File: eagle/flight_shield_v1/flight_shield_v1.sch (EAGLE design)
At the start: 16 parts

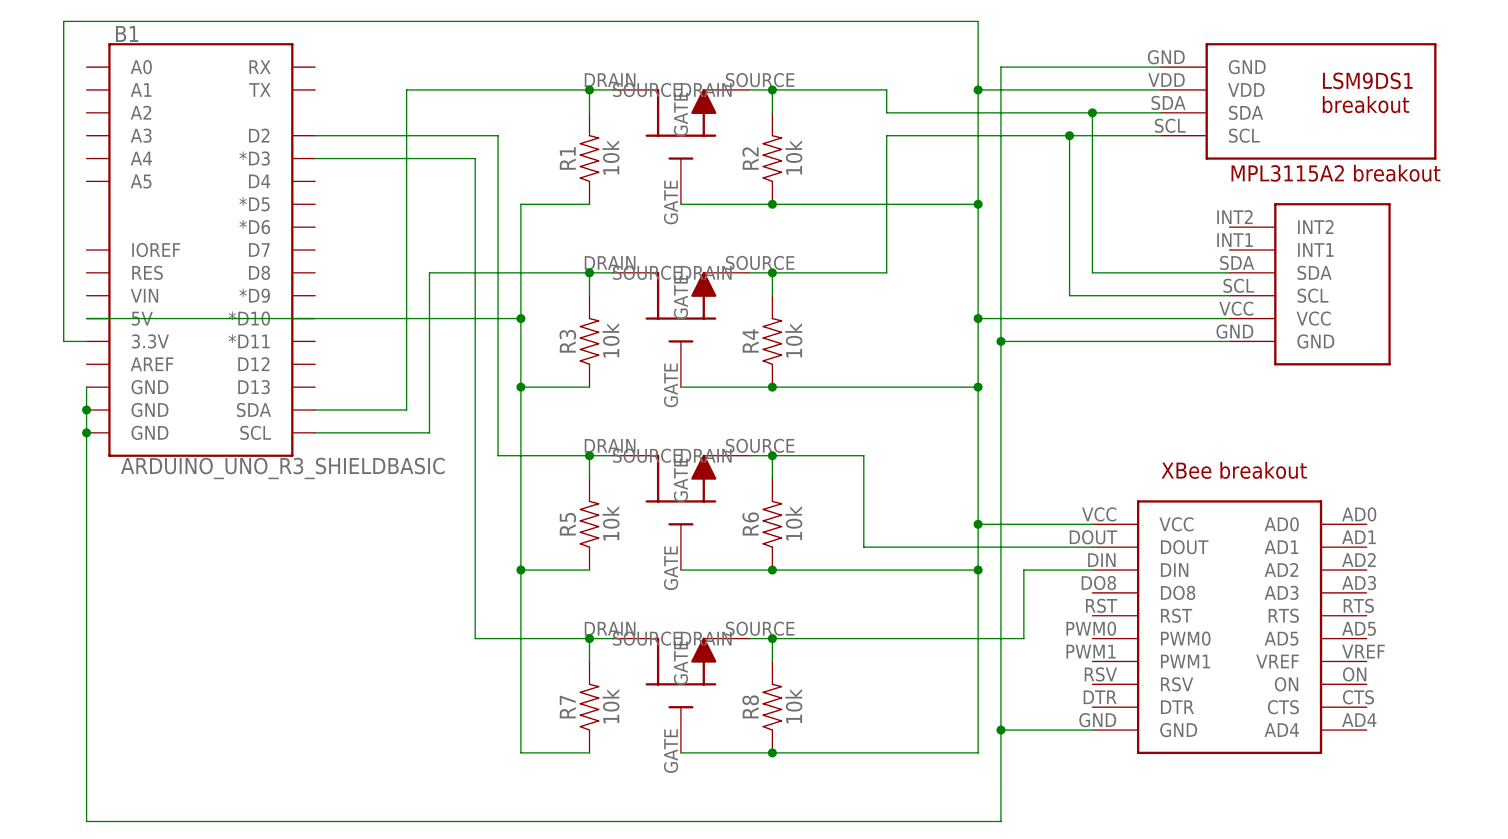
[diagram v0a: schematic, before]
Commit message: IMU / AHRS prosessering begynner å bli bedre. Flyttet arduino filer til git.
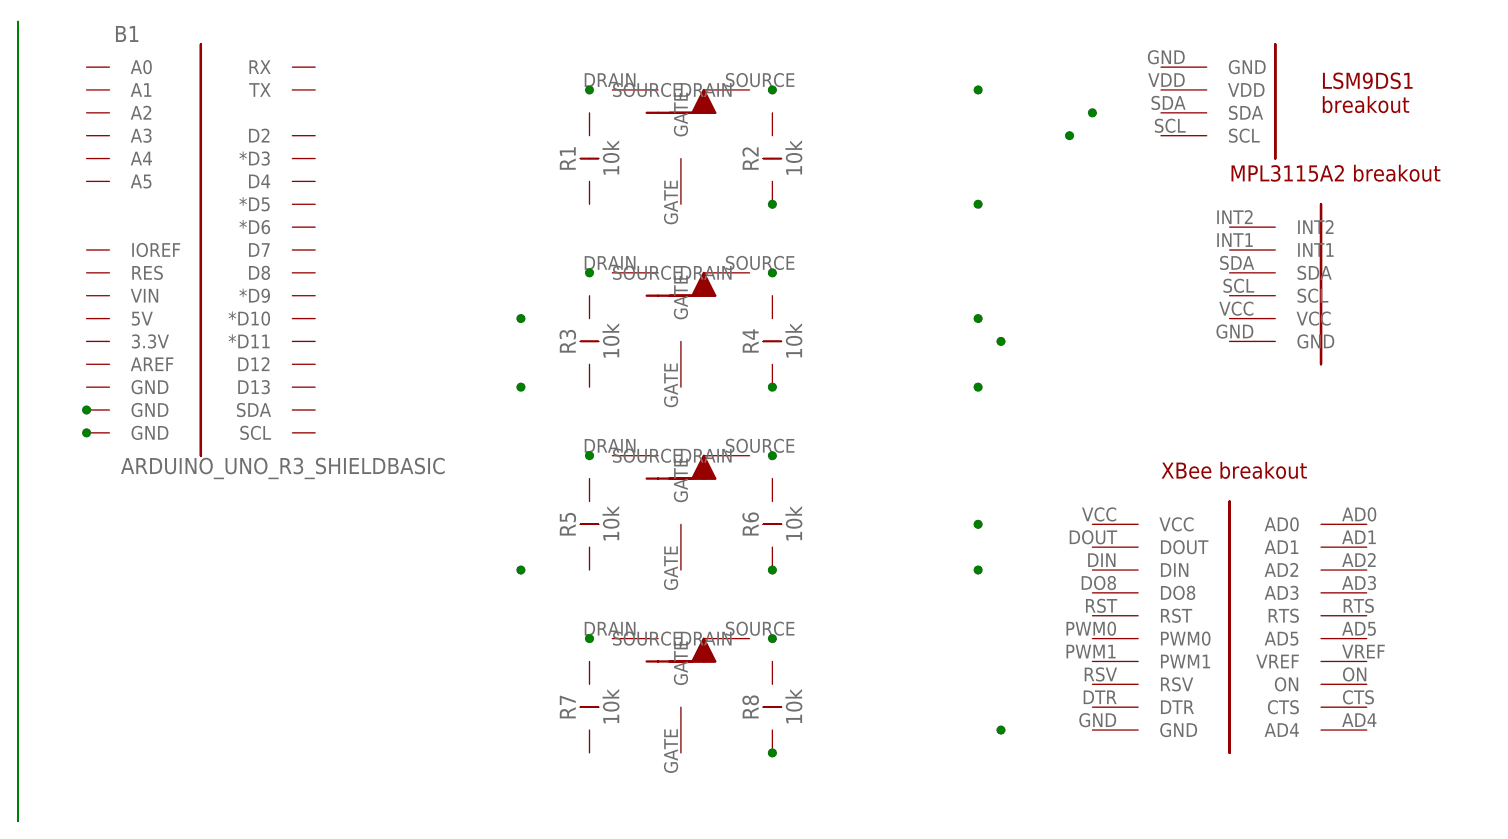
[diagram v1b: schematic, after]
